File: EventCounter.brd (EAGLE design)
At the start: 37.4 x 20.8 mm, 24 parts, among them J1 CONN_42.54_SCREW, Q1 2N7002, Q3 DMG3404, U7 MCP6041, U8 MCP6041

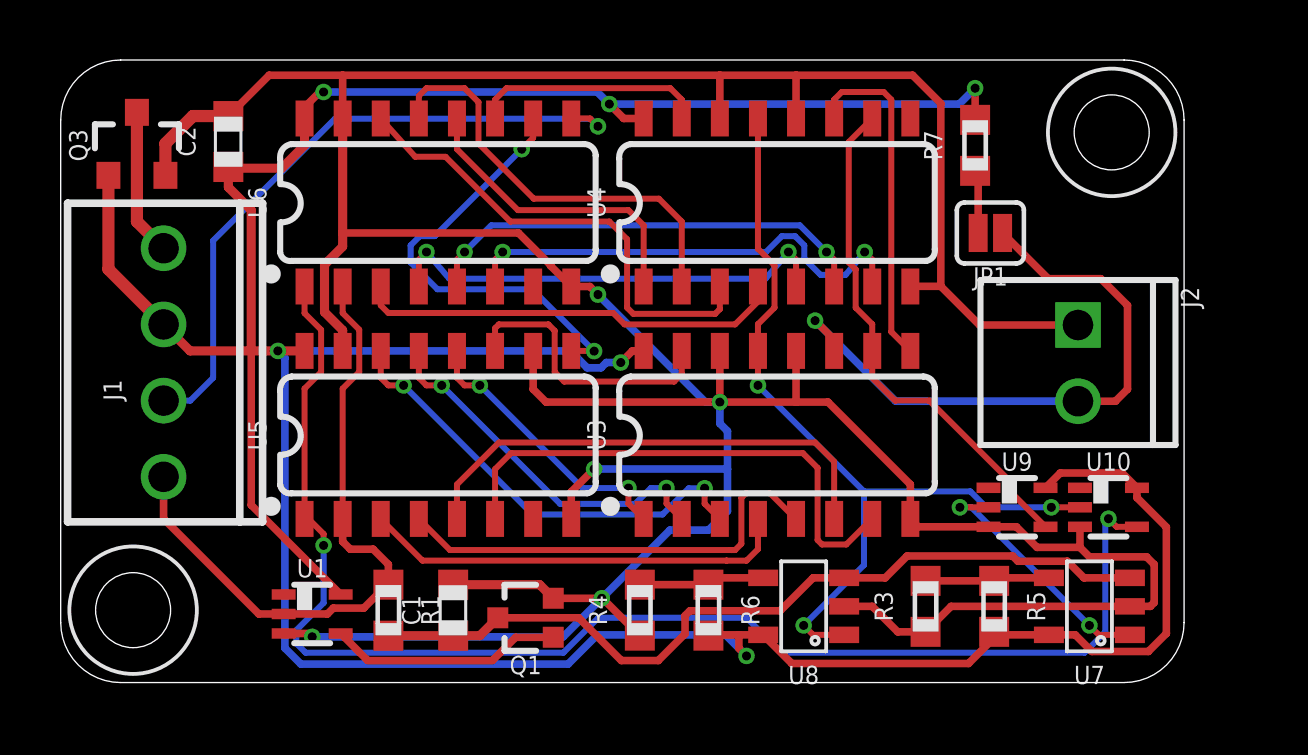
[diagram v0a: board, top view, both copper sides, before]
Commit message: Added input signal conditioning, added test script
Added input signal conditioning to fix metastability problem occurring due to excessive rise times due to pullup input
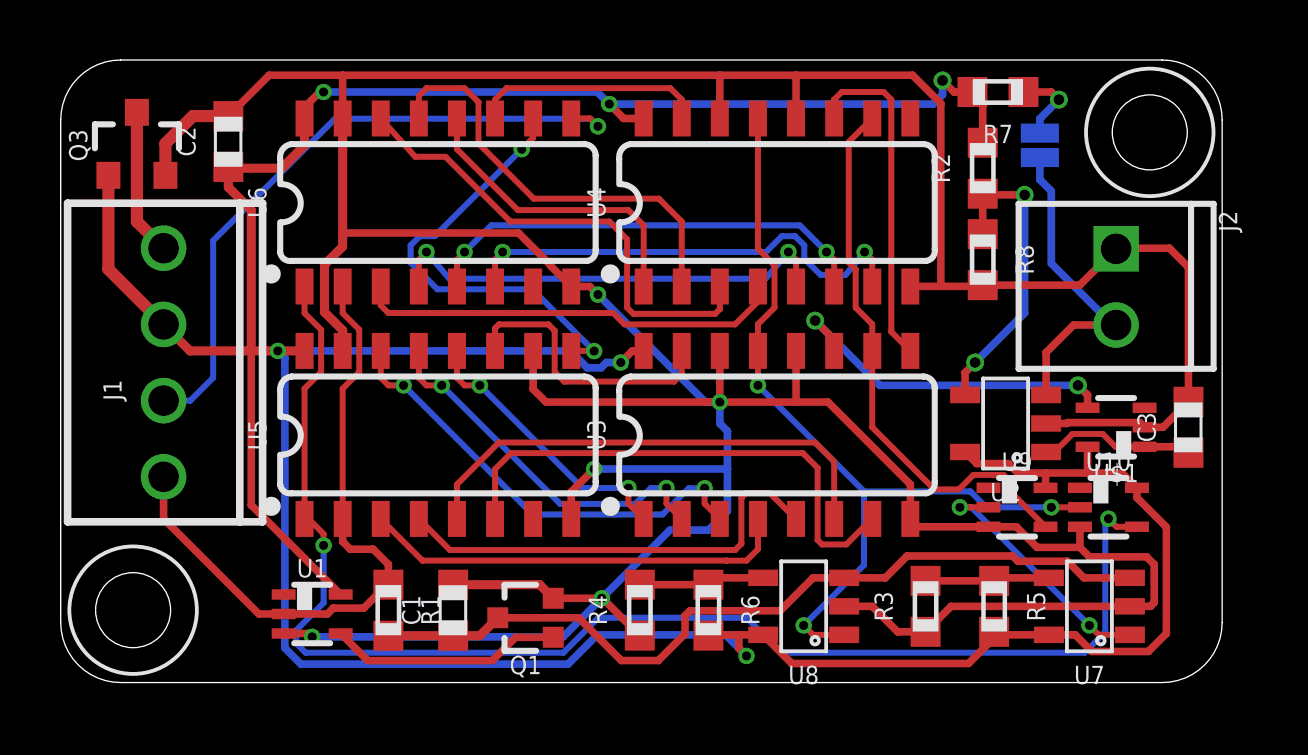
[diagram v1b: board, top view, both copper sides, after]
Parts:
- added C3: 1uF, bschulz_passives:C0603
- added R2: 3.3M, bschulz_passives:R0603
- added R8: 10M, bschulz_passives:R0603
- added U$1: MIC842H, bschulz:DCK_R-PDSO-G5
- added U2: MCP6041, bschulz:SOT23-5
- R7: value 10k -> 3.3M
- moved JP1 3.36 mm to (32.6, 17.9), flipped to the bottom, turned to 90 degrees
- moved J2 2.84 mm to (35.2, 13.2)
- moved R7 1.93 mm to (31.2, 19.7), turned to 180 degrees
- moved H2 1.27 mm to (36.3, 18.3)
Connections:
- new net N$19: R2.1, R8.1, U2.4
- new net N$24: C3.1, U$1.1, U2.1
- new net PULSE_DIG: U$1.4, U3.11
- net GND: now also C3.2, R8.2, U$1.2, U2.2
- net PULSE: now also U2.3; no longer U3.11
- net VCC: now also R2.2, U$1.5, U2.5
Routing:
- net GND: track 143.3 -> 156.9 mm
- net PULSE_DIG: track 0.00 -> 11.8 mm, vias 0 -> 2
- net N$19: track 0.00 -> 10.3 mm, vias 0 -> 2
- net PULSE: track 21.0 -> 10.8 mm, vias 1 -> 0
- net VCC: track 121.2 -> 126.6 mm
- net N$24: track 0.00 -> 5.25 mm
- net !RST: track 17.3 -> 18.7 mm
- net N$20: track 2.11 -> 2.67 mm, vias 0 -> 1
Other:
- board size 37.4 x 20.8 mm -> 38.7 x 20.8 mm
